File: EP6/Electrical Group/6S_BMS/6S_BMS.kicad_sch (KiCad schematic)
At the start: 64 parts, among them J1 BATout, J10 CAN1, J103 battery cells, J11 frontBox, J12 BATcellMain, J2 GLVMS, J3 switch, J4 BAT EXT, Q10 Q_NMOS-D_Generic_GSD, Q11 PMOS, Q12 AO3401A, Q14 2N7002, Q16 2N7002, Q8 PMOS, Q9 2N7002, U2 BQ7693003, U4 78L05G-AB3-R, U5 HT7533

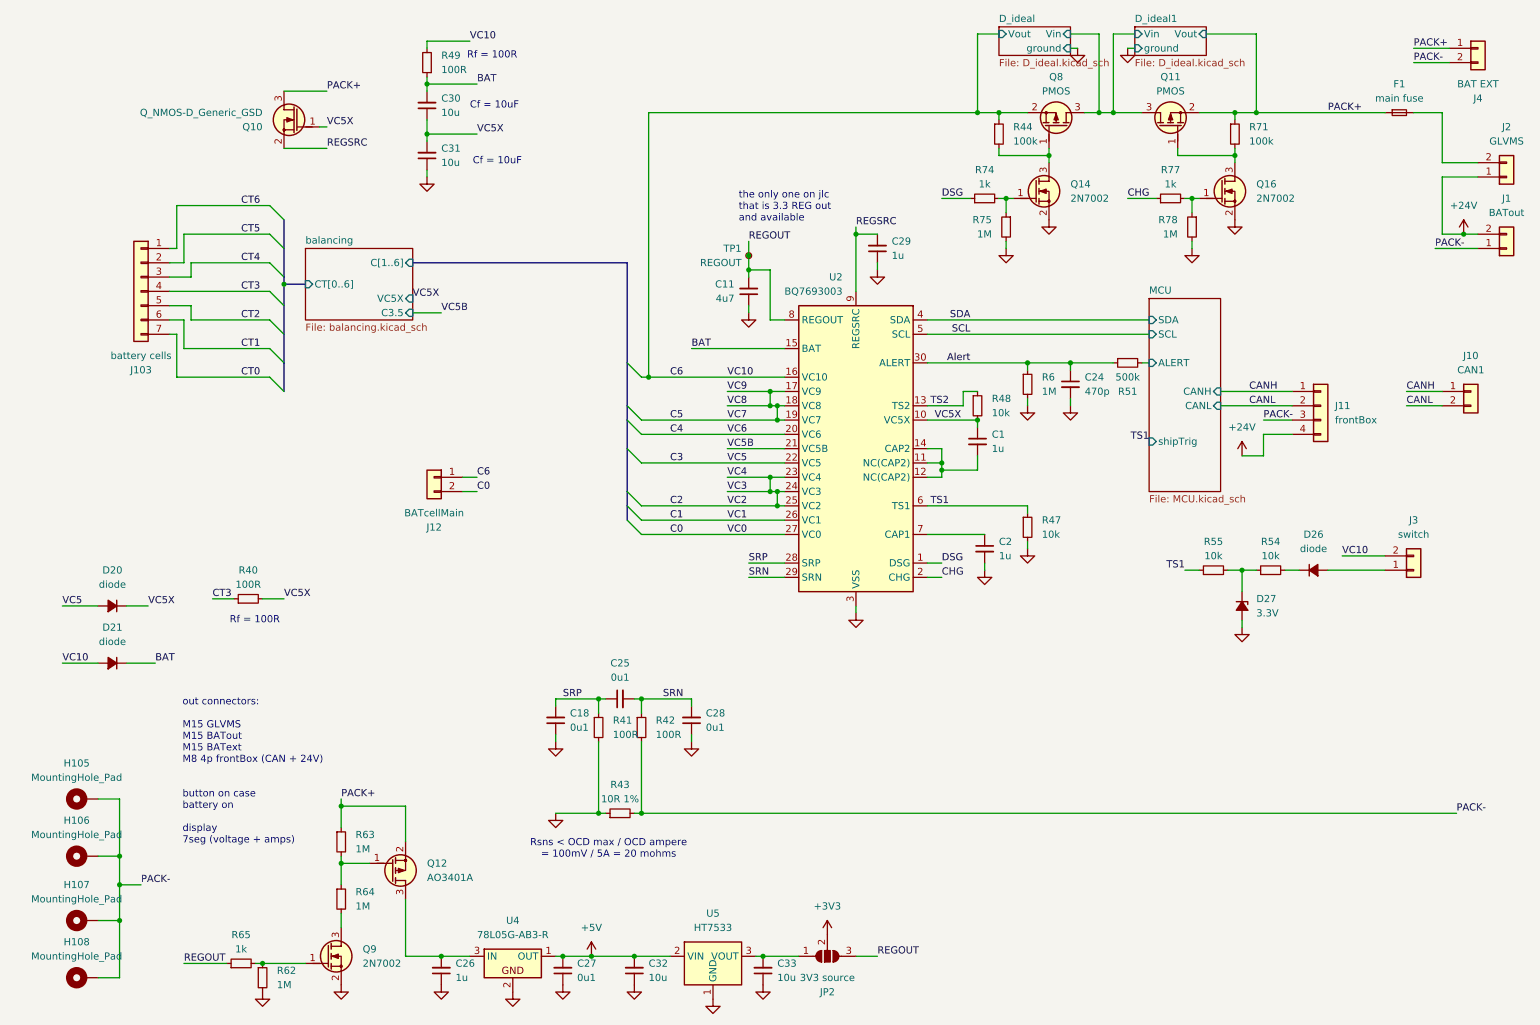
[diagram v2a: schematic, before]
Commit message: update 6S_BMS  schematic and a little layout
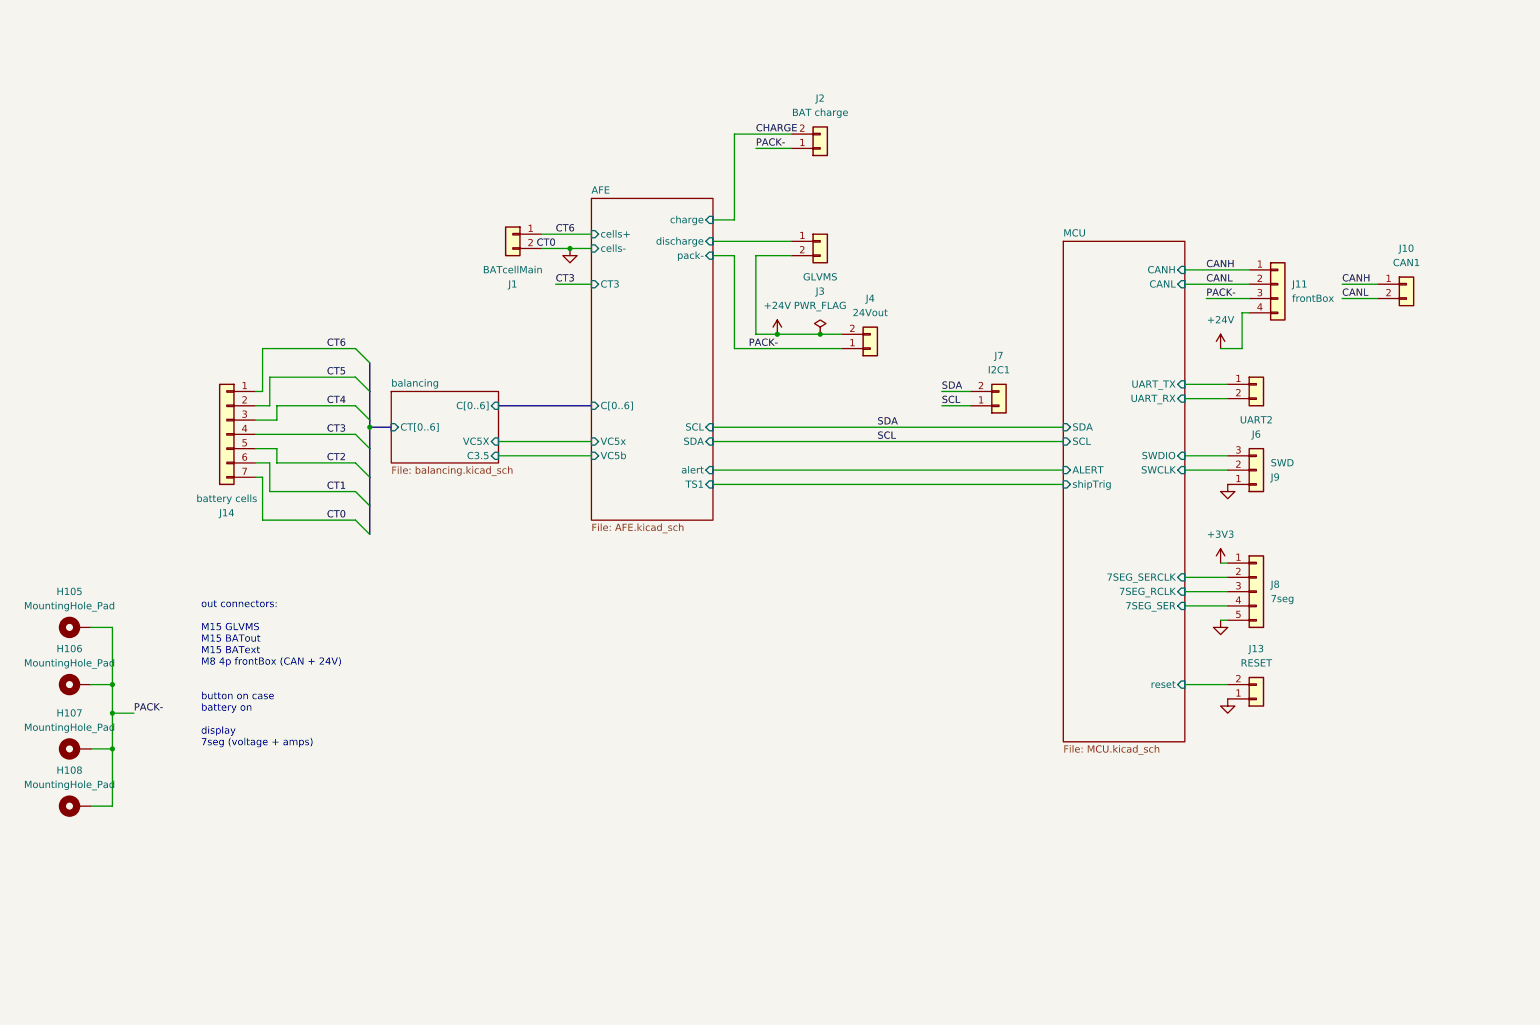
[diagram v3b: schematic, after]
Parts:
- removed C1, C2, C26, C29: 1u, symbol Device:C_Small
- removed C11: 4u7, symbol Device:C_Small
- removed C18, C25, C27, C28: 0u1, symbol Device:C_Small
- removed C24: 470p, symbol Device:C_Small
- removed C30, C31, C32, C33: 10u, symbol Device:C_Small
- removed D20, D21, D26: diode, symbol Device:D_Small_Filled
- removed D27: 3.3V, symbol Device:D_Zener_Small_Filled
- removed F1: main fuse, symbol Device:Fuse_Small
- removed J12: BATcellMain, symbol Connector_Generic:Conn_01x02
- removed JP2: 3V3 source, symbol Jumper:SolderJumper_3_Open
- removed Q10: Q_NMOS-D_Generic_GSD, symbol PCM_Transistor_MOSFET_AKL:Q_NMOS-D_Generic_GSD
- removed Q11, Q8: PMOS, symbol PCM_Transistor_MOSFET_AKL:Q_PMOS-E_Generic_GSD
- removed Q12: AO3401A, PCM_Package_TO_SOT_SMD_AKL:SOT-23, symbol PCM_Transistor_MOSFET_AKL:AO3401A
- removed Q14, Q16, Q9: 2N7002, PCM_Package_TO_SOT_SMD_AKL:SOT-23, symbol PCM_Transistor_MOSFET_AKL:2N7002
- removed R40, R41, R42, R49: 100R, symbol Device:R_Small
- removed R43: 10R 1%, symbol Device:R_Small
- removed R44, R71: 100k, symbol Device:R_Small
- removed R47, R48, R54, R55: 10k, symbol Device:R_Small
- removed R51: 500k, symbol Device:R_Small
- removed R6, R62, R63, R64, R75, R78: 1M, symbol Device:R_Small
- removed R65, R74, R77: 1k, symbol Device:R_Small
- removed TP1: REGOUT, symbol Connector:TestPoint_Small
- removed U2: BQ7693003, Package_SO:TSSOP-30_4.4x7.8mm_P0.5mm, symbol Battery_Management:BQ76930DBT
- removed U4: 78L05G-AB3-R, PCM_Package_TO_SOT_SMD_AKL:SOT-89-3, symbol PCM_Voltage_Regulator_AKL:L78L05ABU
- removed U5: HT7533, Package_TO_SOT_SMD:SOT-89-3, symbol Regulator_Linear:HT75xx-1-SOT89
- added J13: RESET, Connector_JST:JST_XH_S2B-XH-A_1x02_P2.50mm_Horizontal, symbol Connector_Generic:Conn_01x02
- added J6: UART2, Connector_JST:JST_XH_S2B-XH-A_1x02_P2.50mm_Horizontal, symbol Connector_Generic:Conn_01x02
- added J7: I2C1, Connector_JST:JST_XH_S2B-XH-A_1x02_P2.50mm_Horizontal, symbol Connector_Generic:Conn_01x02
- added J8: 7seg, Connector_JST:JST_XH_S5B-XH-A_1x05_P2.50mm_Horizontal, symbol Connector_Generic:Conn_01x05
- added J9: SWD, Connector_JST:JST_XH_S3B-XH-A_1x03_P2.50mm_Horizontal, symbol Connector_Generic:Conn_01x03
- H105, H106, H107, H108: footprint MountingHole:MountingHole_4.3mm_M4_DIN965_Pad_TopBottom -> MountingHole:MountingHole_3.2mm_M3_Pad_TopBottom
- J1: value BATout -> BATcellMain; footprint (none) -> Connector_AMASS:AMASS_XT60PW-M_1x02_P7.20mm_Horizontal
- J11: footprint (none) -> Connector_JST:JST_XH_S4B-XH-A_1x04_P2.50mm_Horizontal
- J14: renamed from J103; footprint Connector_JST:JST_XH_B7B-XH-A_1x07_P2.50mm_Vertical -> Connector_JST:JST_XH_S7B-XH-A_1x07_P2.50mm_Horizontal
- J2: value GLVMS -> BAT charge; footprint (none) -> Connector_AMASS:AMASS_XT60PW-M_1x02_P7.20mm_Horizontal
- J3: value switch -> GLVMS; footprint (none) -> Connector_JST:JST_VH_B2PS-VH_1x02_P3.96mm_Horizontal
- J4: value BAT EXT -> 24Vout; footprint (none) -> Connector_AMASS:AMASS_XT60PW-F_1x02_P7.20mm_Horizontal
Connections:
- net C6 is gone; now on net +24V: J3.2 (Pin_2)
- net CT0 is gone; now on net GND: J14.7 (Pin_7)
- net PACK+ is gone; now on net PACK-: J4.1 (Pin_1)
- net +24V: now also J4.2 (Pin_2); no longer J1.2 (Pin_2), J2.1 (Pin_1)
- net +3V3: now also J8.1 (Pin_1)
- net CT6: now also J1.1 (Pin_1)
- net GND: now also J1.2 (Pin_2), J13.1 (Pin_1), J8.5 (Pin_5), J9.1 (Pin_1)
- net PACK-: now also J2.1 (Pin_1); no longer J1.1 (Pin_1), J4.2 (Pin_2)
- net SCL: now also J7.1 (Pin_1)
- net SDA: now also J7.2 (Pin_2)
- net CHARGE: now reaches J2.2 (Pin_2)
- net AFE/discharge: now reaches J3.1 (Pin_1)
- new net MCU/7SEG_RCLK: J8.3 (Pin_3)
- new net MCU/7SEG_SER: J8.4 (Pin_4)
- new net MCU/7SEG_SERCLK: J8.2 (Pin_2)
- new net MCU/SWCLK: J9.2 (Pin_2)
- new net MCU/SWDIO: J9.3 (Pin_3)
- new net MCU/UART_RX: J6.2 (Pin_2)
- new net MCU/UART_TX: J6.1 (Pin_1)
- new net MCU/reset: J13.2 (Pin_2)
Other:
- removed sheet D_ideal
- removed sheet D_ideal1
- added sheet AFE (AFE.kicad_sch)
- sheet MCU ports: added 7SEG_RCLK, 7SEG_SER, 7SEG_SERCLK, SWCLK, SWDIO, UART_RX, UART_TX, reset; removed none
- sheet balancing ports: added C[0..6]; removed C[1..6]
- note removed: "Cf = 10uF"
- note removed: "Rf = 100R"
- note removed: "Rsns < OCD max / OCD ampere = 100mV / 5A = 20 mohms"
- note removed: "the only one on jlc that is 3.3 REG out and available"
- moved on the sheet: H105, H106, H107, H108, J10, J11, J14
